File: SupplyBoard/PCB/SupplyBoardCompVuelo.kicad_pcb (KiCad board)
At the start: 2 copper layers, 99 x 99 mm, 149 parts, among them J1 Conn_01x02, J2 NebulaConnector, J3 Conn_01x04, J4 Conn_01x03, SW1 SW_SPDT, SW2 RESET, SW3 SW_SPDT, U1 STM32L031F6Px, U10 INA2180A2, U11 INA2180A2, U12 INA2180A2, U2 LD39200DPUR, U3 LD39200DPUR, U4 LD39200DPUR, U5 LD39200DPUR, U6 TPS5430DDA, U7 TPS5430DDA, U8 TPS5430DDA, U9 LD39200DPUR, Y1 16Mhz

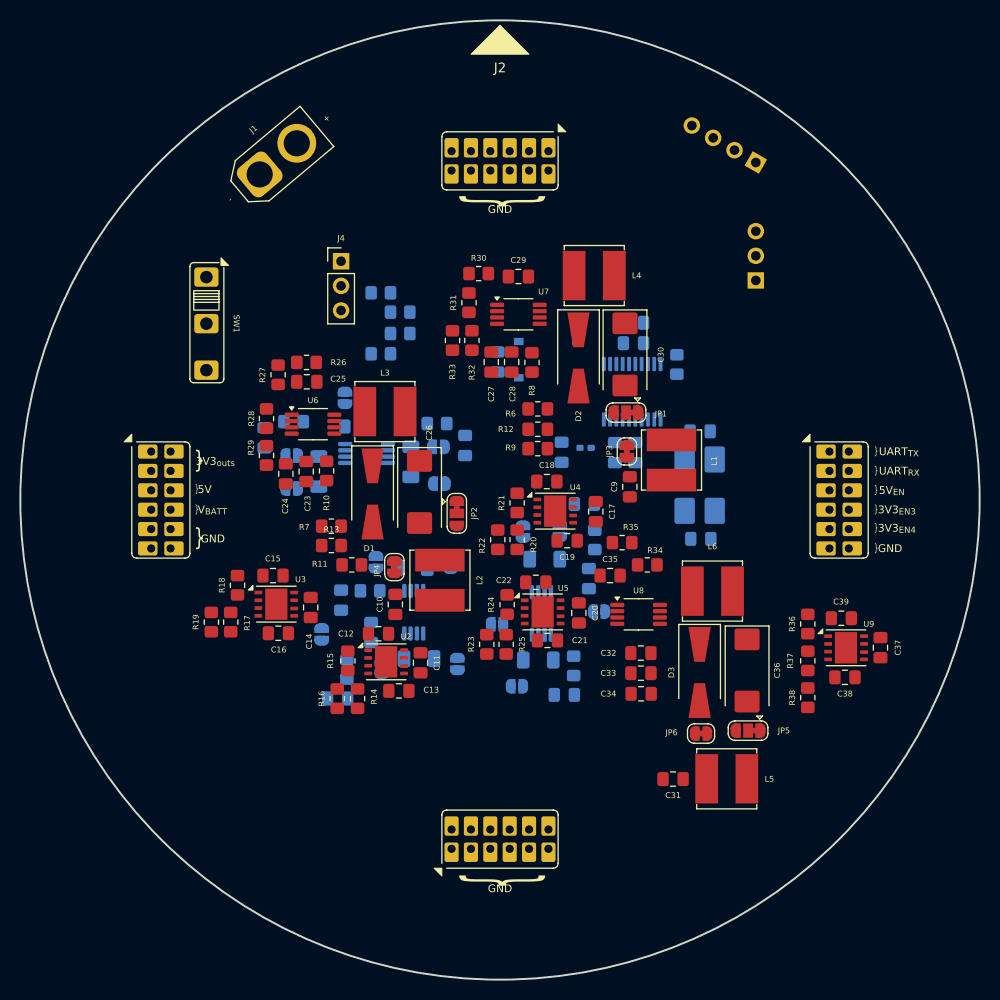
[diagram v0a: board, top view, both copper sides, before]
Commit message: Supply Board & Folder Organization
Reorganization of the power supply board components, simplifying the layout to facilitate future debugging and reorganizing some folders and documents, as well as adding the power supply board schematic; in supply board only need to make the routing
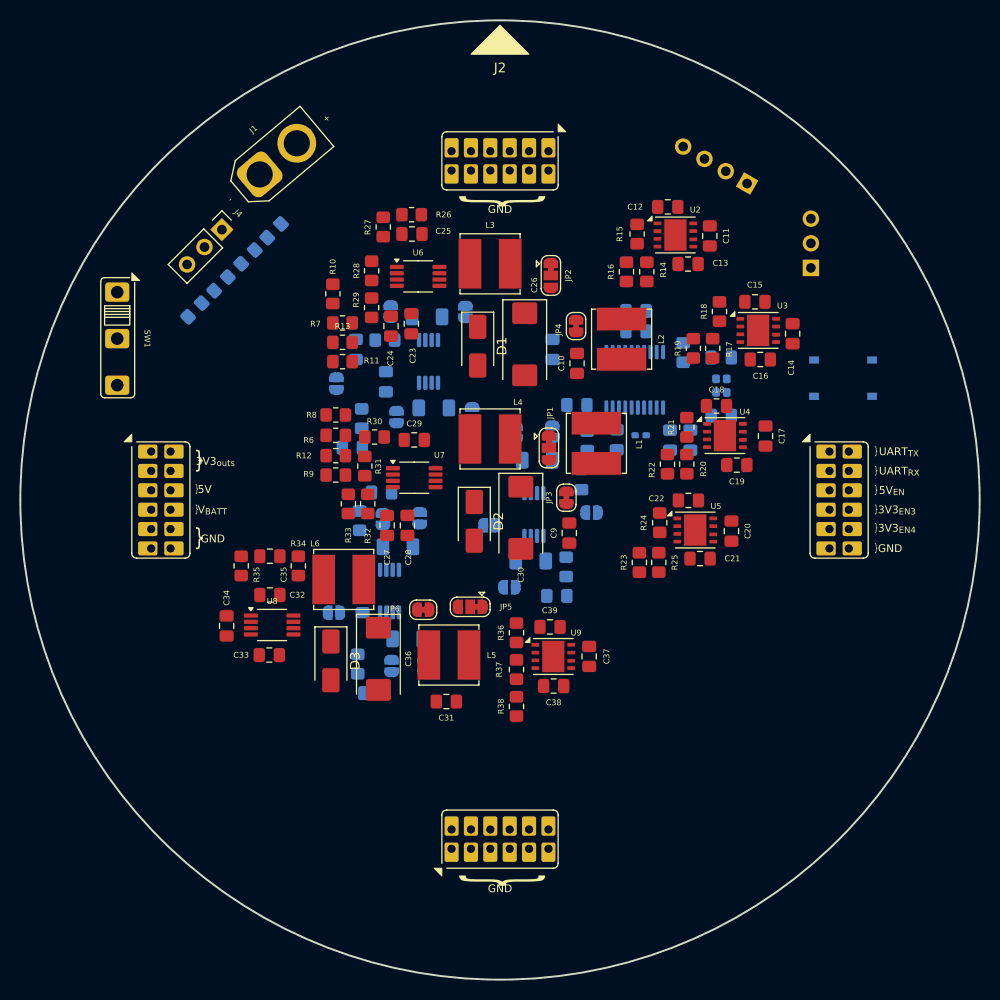
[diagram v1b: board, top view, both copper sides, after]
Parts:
- D1, D2, D3: footprint Diode_SMD:D_SMA-SMB_Universal_Handsoldering -> Diode_SMD:D_SMA
- Y1: footprint Crystal:Crystal_SMD_0603-4Pin_6.0x3.5mm_HandSoldering -> Crystal:Crystal_SMD_2016-4Pin_2.0x1.6mm
- moved C14 57.2 mm to (129.3, 77.4)
- moved C16 57.2 mm to (126.0, 80.1)
- moved C15 57.2 mm to (125.4, 74.2)
- moved R17 57.2 mm to (121.0, 79.0)
- moved R18 57.2 mm to (121.8, 75.2)
- moved R19 57.2 mm to (119.0, 79.0)
- moved U3 57.2 mm to (125.8, 77.2)
- moved C13 53.2 mm to (118.5, 70.2)
- moved R16 53.2 mm to (112.2, 71.0)
- moved U2 53.2 mm to (117.2, 67.3)
- moved C11 53.2 mm to (120.8, 67.3)
- moved C12 53.2 mm to (116.4, 64.3)
- moved R14 53.2 mm to (114.2, 71.0)
- moved R15 53.2 mm to (113.2, 67.2)
- moved C34 43.3 mm to (70.9, 107.6), turned to 90 degrees
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
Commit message: Supply & Coms-Sensor Board
la organizacion de los componentes presentes en las placas, se quedaran de esa manera, se espera que en la serigrafia se incluyan los logos de los patrocinadores, ademas se incluyo la carpeta 3D la cual contiene modelos en 3D de las dos placas, con serigrafia y componentes incluidos y ya
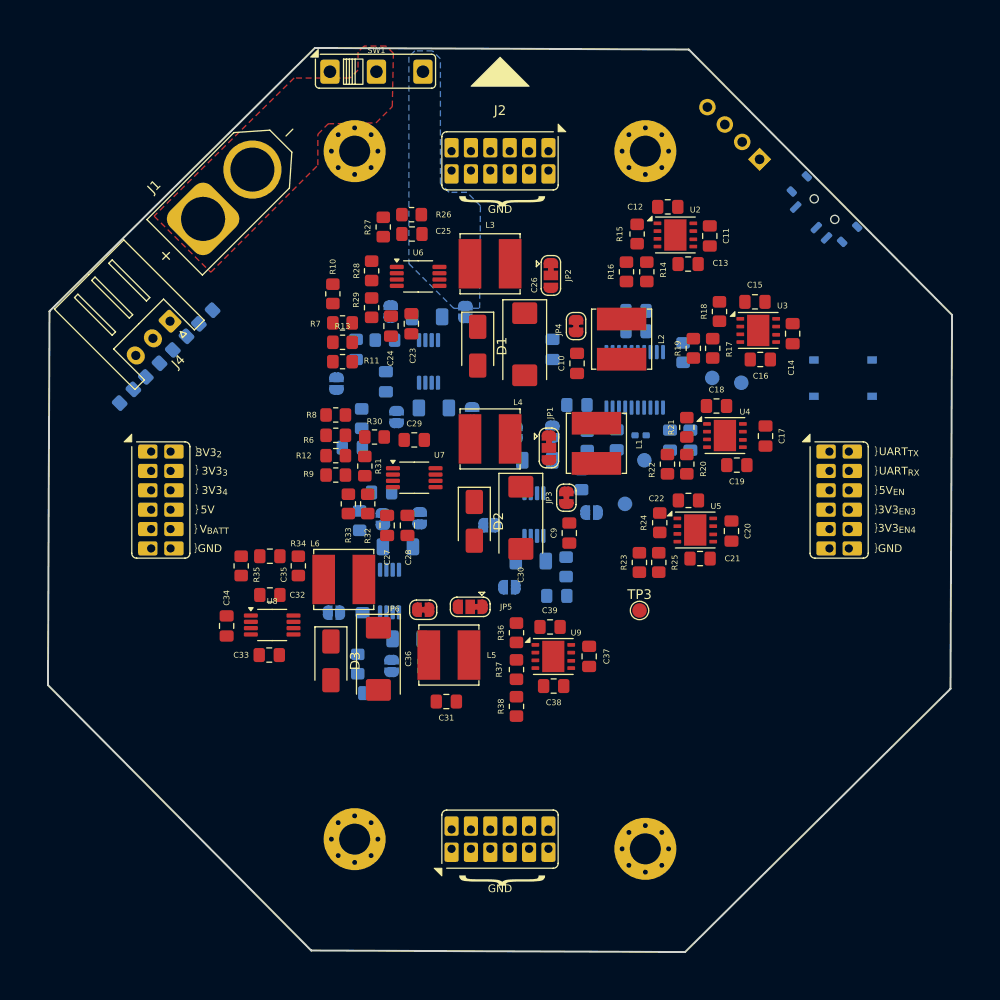
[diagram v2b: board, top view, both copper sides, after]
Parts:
- removed C2, C5: 9pF, Capacitor_SMD:C_0805_2012Metric_Pad1.18x1.45mm_HandSolder
- removed Y1: 16Mhz, Crystal:Crystal_SMD_2016-4Pin_2.0x1.6mm
- added TP1: TestPoint, TestPoint:TestPoint_Pad_D1.5mm, B.Cu at (114.0, 90.5)
- added TP2: TestPoint, TestPoint:TestPoint_Pad_D1.5mm, B.Cu at (112.0, 95.0)
- added TP3: TestPoint, TestPoint:TestPoint_Pad_D1.5mm, F.Cu at (113.5, 106.0)
- added TP4: TestPoint, TestPoint:TestPoint_Pad_D1.5mm, B.Cu at (121.0, 82.0)
- added TP5: TestPoint, TestPoint:TestPoint_Pad_D1.5mm, B.Cu at (124.0, 82.5)
- J1: value Conn_01x02 -> XT60-M; footprint Connector_AMASS:AMASS_XT30U-F_1x02_P5.0mm_Vertical -> CompVuelo:AMASS_XT60-M
- J4: footprint Connector_PinHeader_2.54mm:PinHeader_1x03_P2.54mm_Vertical -> Connector_JST:JST_XH_S3B-XH-A_1x03_P2.50mm_Horizontal
- SW3: footprint Connector_PinHeader_2.54mm:PinHeader_1x03_P2.54mm_Vertical -> Button_Switch_SMD:SW_SPDT_Shouhan_MSK12C02
- moved SW1 38.4 mm to (86.3, 50.4), turned to 0 degrees
- moved R5 11.4 mm to (60.6, 83.9)
- moved R2 11.4 mm to (68.7, 75.7)
- moved R3 11.4 mm to (66.0, 78.4)
- moved R4 11.4 mm to (63.3, 81.2)
- moved J4 10.9 mm to (65.0, 76.2), turned to -135 degrees
- moved SW3 6.23 mm to (132.6, 64.6), turned to -45 degrees
- moved J1 3.88 mm to (71.0, 63.0), turned to 45 degrees
- moved J3 2.81 mm to (125.9, 59.4), turned to 45 degrees
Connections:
- U1 pad 2: OSC_IN -> unconnected-(U1-PC14-Pad2)
- U1 pad 3: OSC_OUT -> unconnected-(U1-PC15-Pad3)
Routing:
- added copper zone on B.Cu, net +7.4V
- added copper zone on F.Cu, net +BATT
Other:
- board size 99 x 99 mm -> 93.3 x 93.3 mm
